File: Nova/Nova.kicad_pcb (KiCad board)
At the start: 4 copper layers, 38.1 x 100.1 mm, 103 parts, among them J1 Conn_01x06_Male, J2 Conn_02x04_Counter_Clockwise, J4 Conn_01x02_Female, J5 Conn_01x04_Female, J6 Conn_01x04_Female, J7 USB_C_Receptacle_USB2.0, Q1 Q_NMOS_DGS, Q2 Q_NMOS_DGS, Q3 Q_NMOS_DGS, Q4 Q_NMOS_DGS, Q5 Q_NMOS_DGS, Q6 Q_NMOS_DGS, Q7 Q_NMOS_DGS, Q8 Q_NMOS_DGS, Q9 Q_NMOS_DGS, U1 STM32F411CEUx, U2 ST_H3LIS331DL, U3 WB_W25N512GVPIT, U4 FT230XQ, U5 OP179GRT, U6 TE_MS560702BA03-50, U7 MPU-9250, U8 NCP1117-3.3_TO252, Y1 32.768kHz, Y2 25MHz

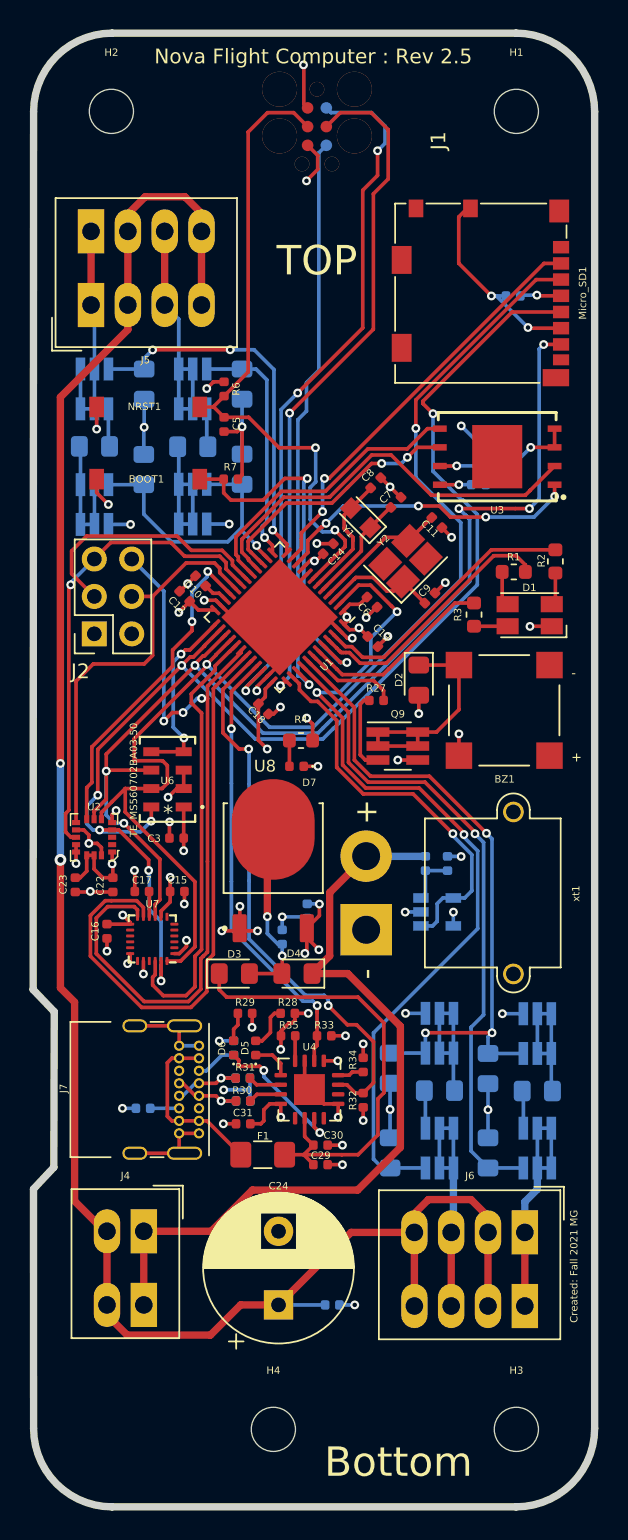
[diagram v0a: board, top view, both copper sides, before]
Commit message: Fixed Dumb and Dumber (Pins 2 and 3)
Sorry again yall, but it's good now lol
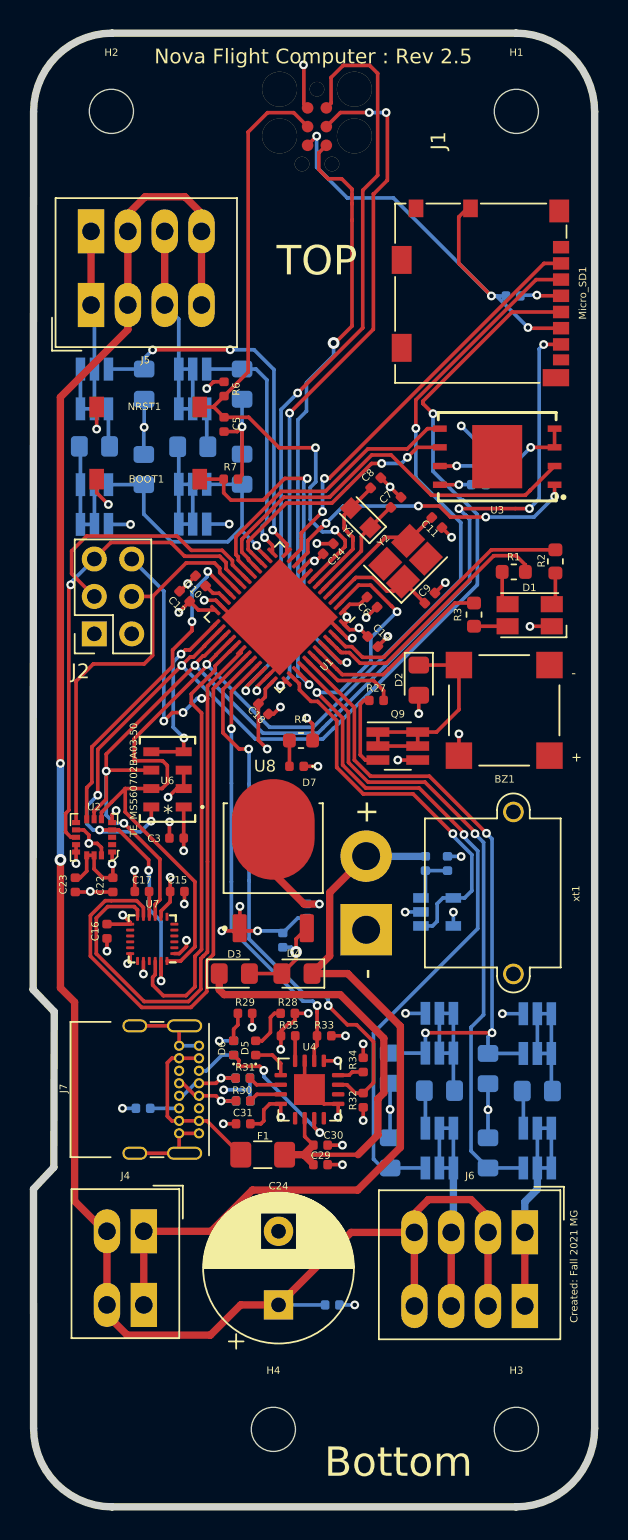
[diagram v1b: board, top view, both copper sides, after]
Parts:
- moved C1 0.22 mm to (157.6, 105.3)
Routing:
- net GND: track 135.3 -> 152.1 mm, vias 51 -> 50
- net Net-(C1-Pad2): track 12.8 -> 7.01 mm, vias 2 -> 1
- net /SWDIO: track 48.6 -> 53.4 mm, vias 3 -> 2
- net /SWO: track 39.1 -> 41.6 mm, vias 1 -> 2
- net +3V3: track 72.2 -> 73.6 mm, vias 32 -> 30
- net /SWCLK: track 46.4 -> 47.1 mm, vias 2 -> 4
- net VBUS: track 31.8 -> 31.2 mm
